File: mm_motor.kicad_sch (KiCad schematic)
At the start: 1 part, among them M1 N20_encoder

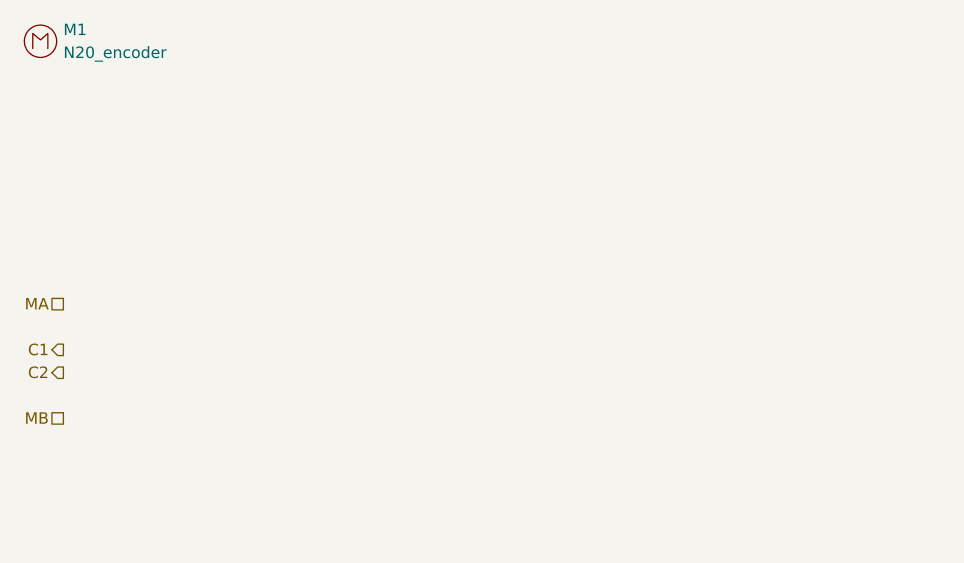
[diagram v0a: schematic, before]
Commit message: ended PCB + added reverse voltage protection
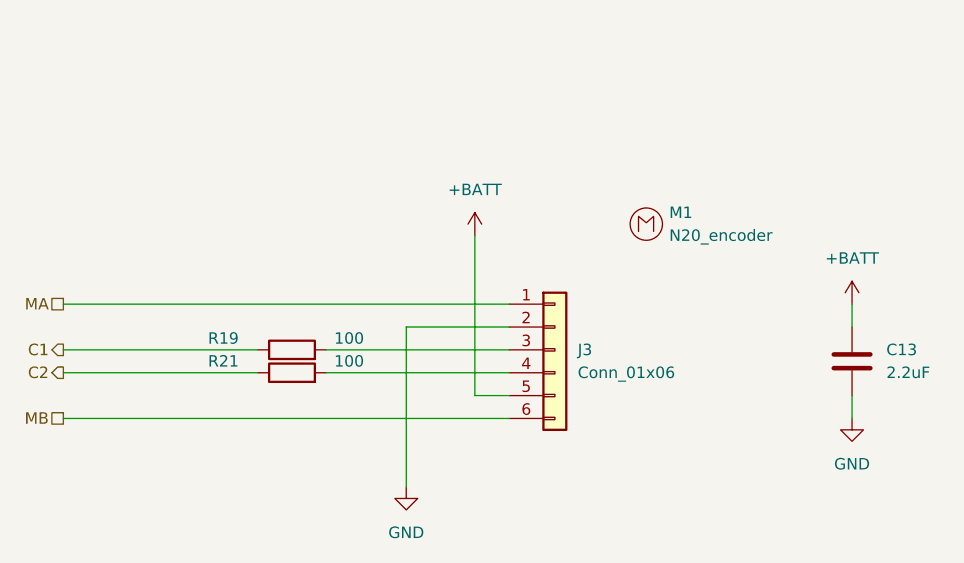
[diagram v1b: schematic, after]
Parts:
- added C13: 2.2uF, Capacitor_SMD:C_0603_1608Metric, symbol Device:C
- added J3: Conn_01x06, Connector_PinHeader_2.54mm:PinHeader_1x06_P2.54mm_Vertical, symbol Connector_Generic:Conn_01x06
- added R19, R21: 100, Resistor_SMD:R_0603_1608Metric, symbol Device:R
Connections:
- net C1: now also R19.1
- net C2: now also R21.1
- net MA: now also J3.1 (Pin_1)
- net MB: now also J3.6 (Pin_6)
- new net: J3.4 (Pin_4), R21.2
- new net: J3.3 (Pin_3), R19.2
- new net +BATT: C13.1, J3.5 (Pin_5)
- new net GND: C13.2, J3.2 (Pin_2)
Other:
- moved on the sheet: M1
